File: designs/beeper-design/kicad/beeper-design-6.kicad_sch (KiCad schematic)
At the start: 23 parts, among them U3 BQ51003YFPR, U5 FH19C-6S-0.5SH(10)

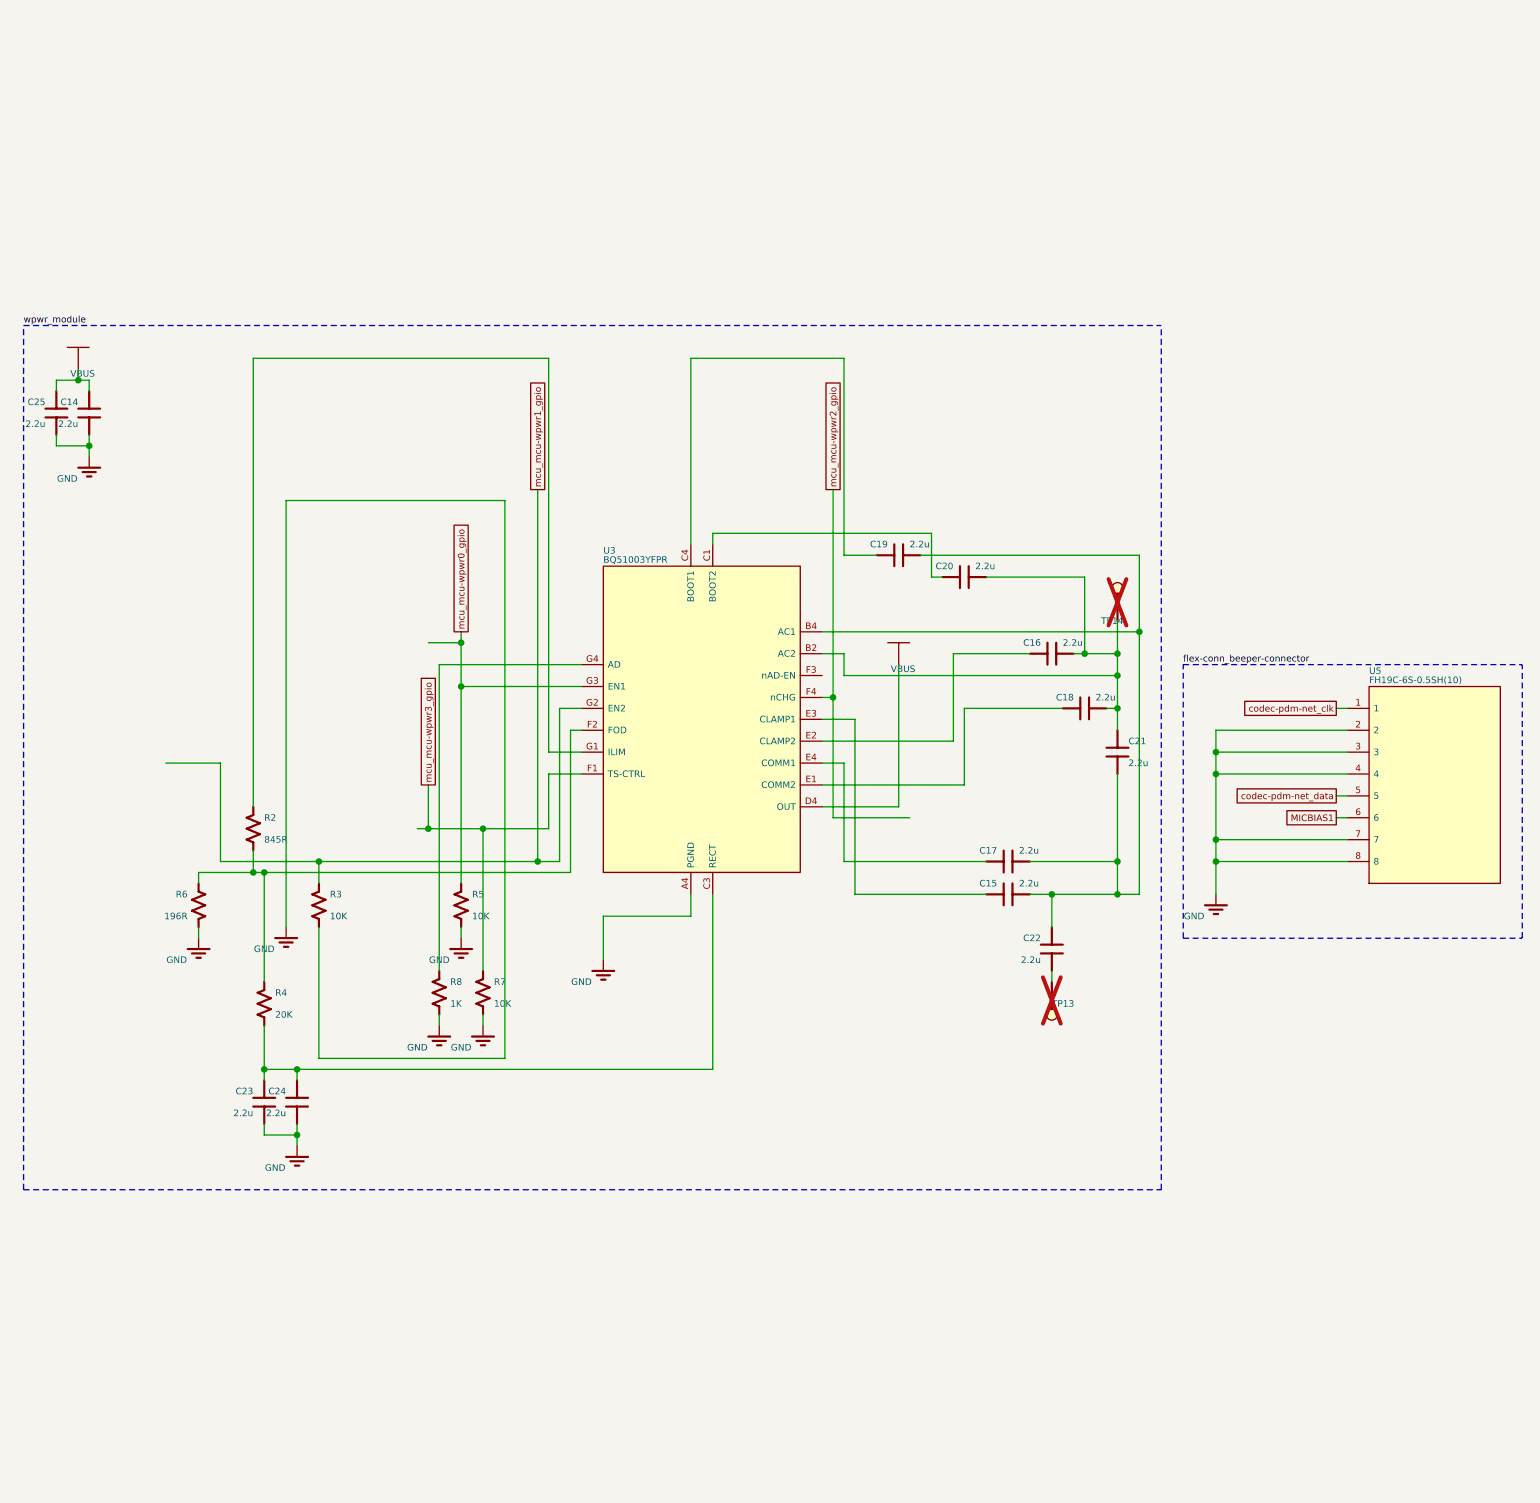
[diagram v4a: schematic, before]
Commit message: exported, yet XTALM32p keeps disappearing
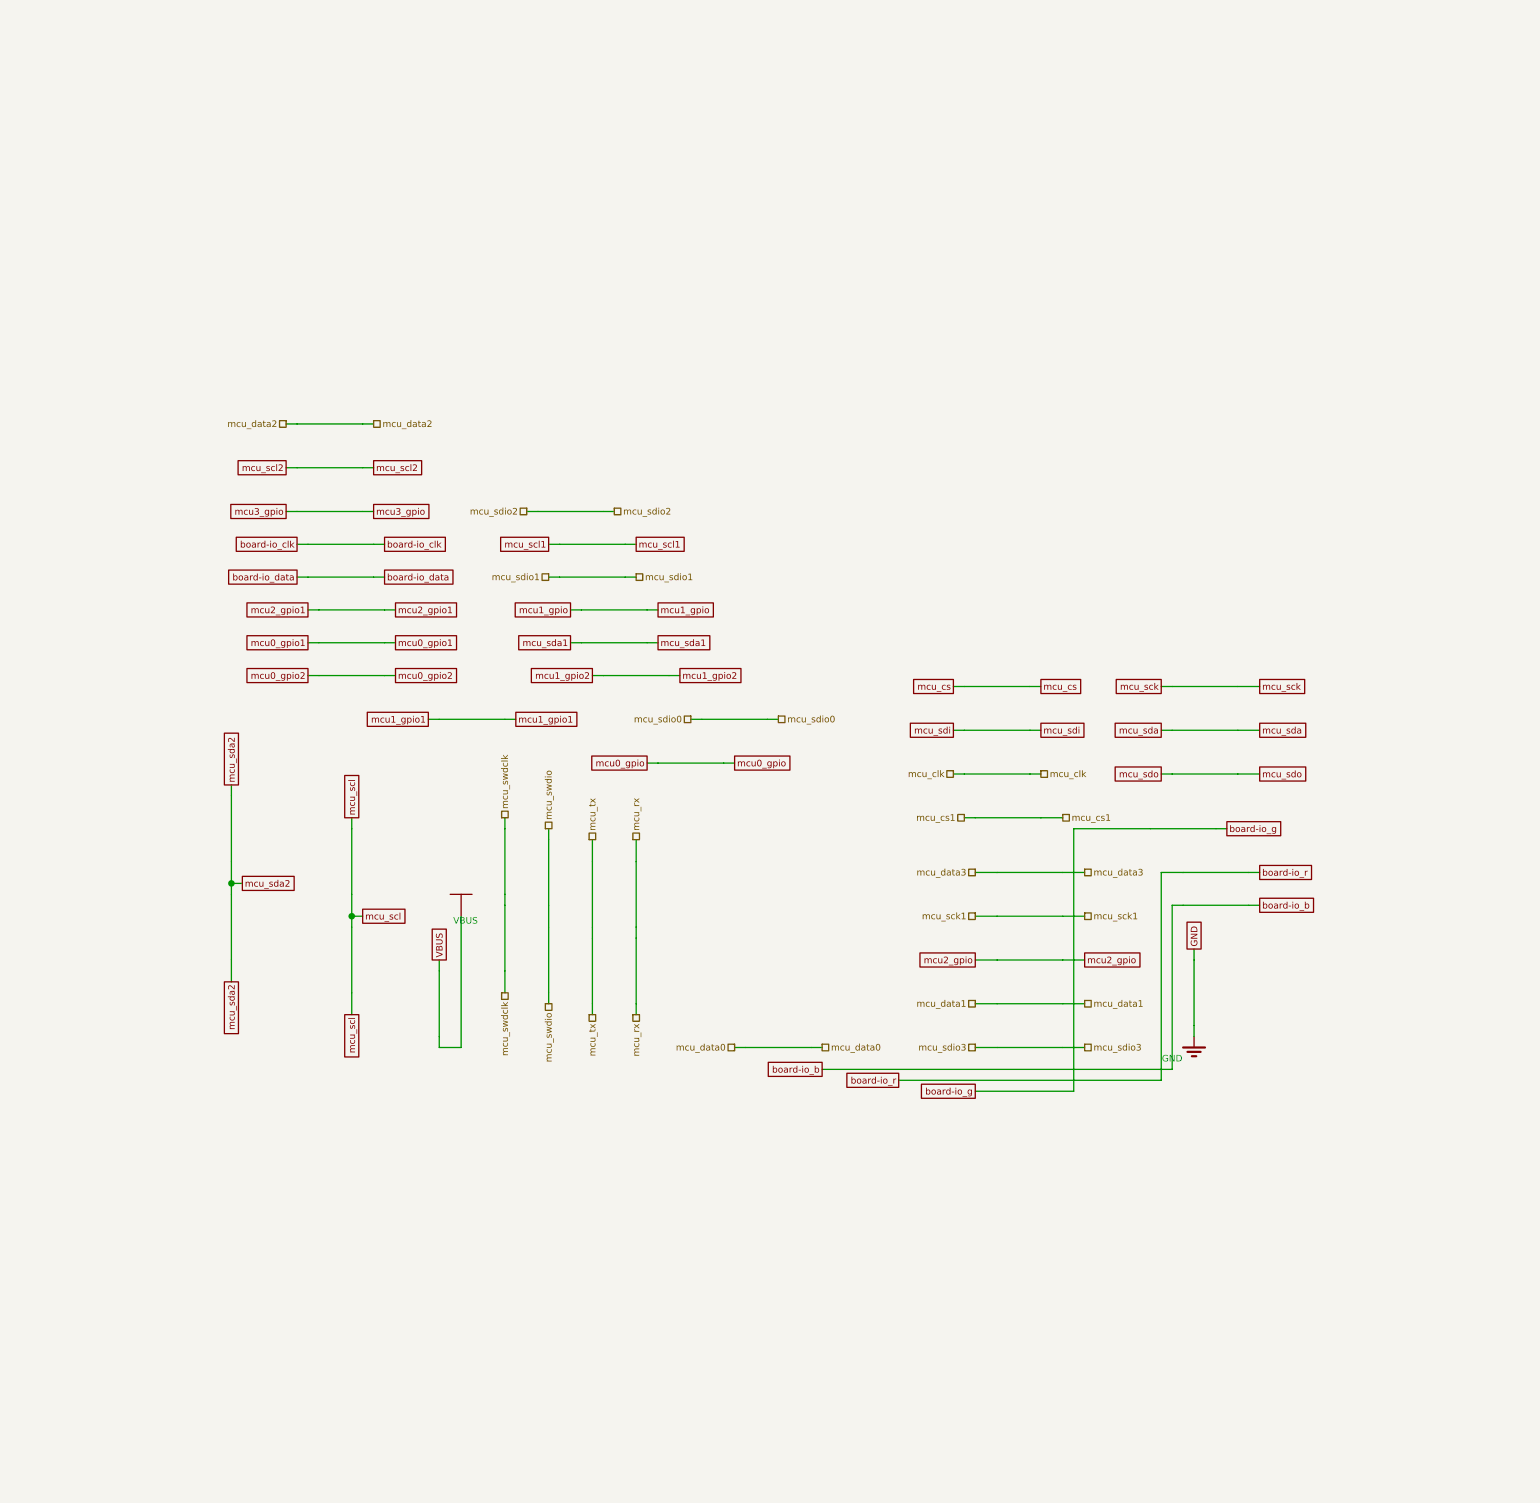
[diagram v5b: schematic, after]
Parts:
- removed C14: 2.2u, beeper-design:Pkg0201, symbol C335106_35
- removed C15: 2.2u, beeper-design:Pkg0201_50, symbol C335106_31
- removed C16: 2.2u, beeper-design:Pkg0201_9, symbol C335106_7
- removed C17: 2.2u, beeper-design:Pkg0201_22, symbol C335106_14
- removed C18: 2.2u, beeper-design:Pkg0201_36, symbol C335106_22
- removed C19: 2.2u, beeper-design:Pkg0201_49, symbol C335106_30
- removed C20: 2.2u, beeper-design:Pkg0201_7, symbol C335106_5
- removed C21: 2.2u, beeper-design:Pkg0201_20, symbol C335106_12
- removed C22: 2.2u, beeper-design:Pkg0201_33, symbol C335106_20
- removed C23: 2.2u, beeper-design:Pkg0201_48, symbol C335106_29
- removed C24: 2.2u, beeper-design:Pkg0201_6, symbol C335106_4
- removed C25: 2.2u, beeper-design:Pkg0201_18, symbol C335106_11
- removed R2: 845R, beeper-design:Pkg0201_15, symbol my_resistor_3
- removed R3: 10K, beeper-design:Pkg0201_10, symbol my_resistor
- removed R4: 20K, beeper-design:Pkg0201_40, symbol my_resistor_11
- removed R5: 10K, beeper-design:Pkg0201_52, symbol my_resistor_14
- removed R6: 196R, beeper-design:Pkg0201_27, symbol C138167
- removed R7: 10K, beeper-design:Pkg0201_23, symbol my_resistor_6
- removed R8: 1K, beeper-design:Pkg0201_38, symbol my_resistor_10
- removed TP13, TP14: (no value), beeper-design:SMD_TESTPT, symbol smd_testpoint_cmp
- removed U3: BQ51003YFPR, beeper-design:LP_6, symbol BQ51003YFPR
- removed U5: FH19C-6S-0.5SH(10), beeper-design:LP_4, symbol FH19C_6S_0_5SH_10_
